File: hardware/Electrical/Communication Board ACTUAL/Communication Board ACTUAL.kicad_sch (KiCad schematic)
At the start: 14 parts, among them J1 CC1101 Radio, J2 Camera, J3 MCP9808 Temperature Sensor, Q1 2N2222, U1 STM32F411CEUx

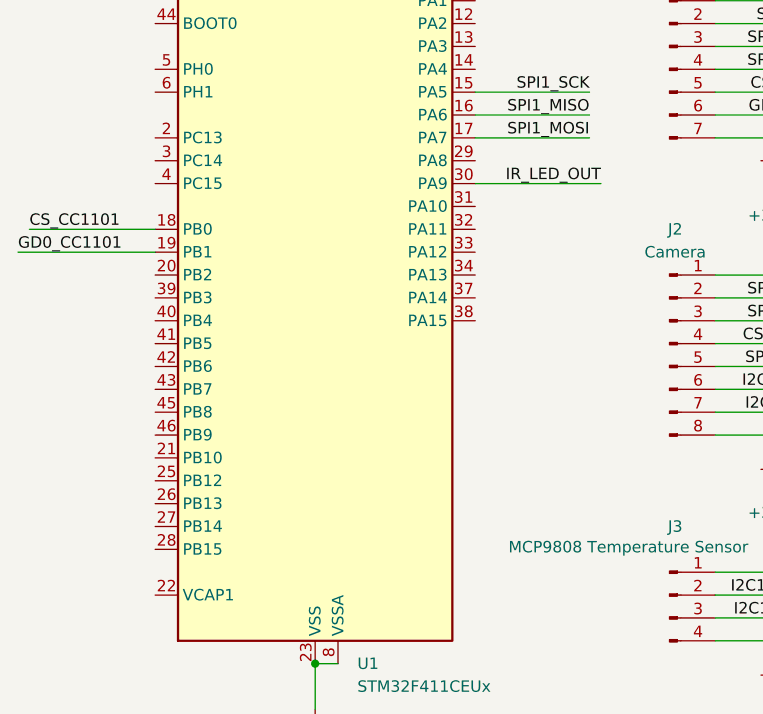
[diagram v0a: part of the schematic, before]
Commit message: changed comm board pin labels
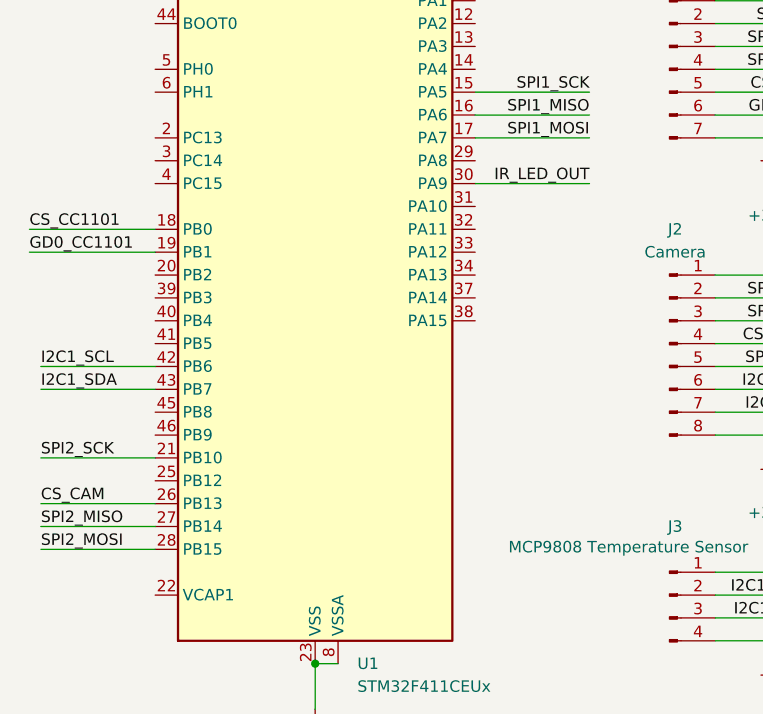
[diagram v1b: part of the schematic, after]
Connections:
- net CS_CAM: now also U1.26 (PB13)
- net I2C1_SCL: now also U1.42 (PB6)
- net I2C1_SDA: now also U1.43 (PB7)
- net SPI2_MISO: now also U1.27 (PB14)
- net SPI2_MOSI: now also U1.28 (PB15)
- net SPI2_SCK: now also U1.21 (PB10)
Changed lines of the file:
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@@
 	(wire
 		(pts
-			(xy 133.35 86.36) (xy 119.38 86.36)
+			(xy 132.08 86.36) (xy 119.38 86.36)
 		)
 		(stroke
@@
 	(wire
 		(pts
+			(xy 71.12 124.46) (xy 83.82 124.46)
+		)
+		(stroke
+			(width 0)
+			(type default)
+		)
+	)
+	(wire
+		(pts
 			(xy 152.4 114.3) (xy 152.4 116.84)
 		)
@@
 	(wire
 		(pts
+			(xy 71.12 121.92) (xy 83.82 121.92)
+		)
+		(stroke
+			(width 0)
+			(type default)
+		)
+	)
+	(wire
+		(pts
 			(xy 96.52 55.88) (xy 99.06 55.88)
 		)
@@
 	(wire
 		(pts
+			(xy 71.12 109.22) (xy 83.82 109.22)
+		)
+		(stroke
+			(width 0)
+			(type default)
+		)
+	)
+	(wire
+		(pts
 			(xy 101.6 139.7) (xy 101.6 144.78)
 		)
@@
 	(wire
 		(pts
+			(xy 71.12 116.84) (xy 83.82 116.84)
+		)
+		(stroke
+			(width 0)
+			(type default)
+		)
+	)
+	(wire
+		(pts
 			(xy 201.93 80.01) (xy 204.47 80.01)
 		)
@@
 	(wire
 		(pts
-			(xy 68.58 93.98) (xy 83.82 93.98)
+			(xy 69.85 93.98) (xy 83.82 93.98)
 		)
 		(stroke
@@
 	(wire
 		(pts
+			(xy 71.12 106.68) (xy 83.82 106.68)
+		)
+		(stroke
+			(width 0)
+			(type default)
+		)
+	)
+	(wire
+		(pts
 			(xy 99.06 55.88) (xy 101.6 55.88)
 		)
@@
 		(pts
 			(xy 195.58 121.92) (xy 195.58 124.46)
+		)
+		(stroke
+			(width 0)
+			(type default)
+		)
+	)
+	(wire
+		(pts
+			(xy 71.12 127) (xy 83.82 127)
 		)
 		(stroke
@@
 	)
 	(label "GD0_CC1101"
-		(at 68.58 93.98 0)
+		(at 69.85 93.98 0)
 		(effects
 			(font
@@
 		)
 	)
+	(label "SPI2_MOSI"
+		(at 71.12 127 0)
+		(effects
+			(font
+				(size 1.27 1.27)
+			)
+			(justify left bottom)
+		)
+	)
 	(label "SPI1_SCK"
 		(at 132.08 76.2 180)
@@
 		)
 	)
+	(label "I2C1_SDA"
+		(at 71.12 109.22 0)
+		(effects
+			(font
+				(size 1.27 1.27)
+			)
+			(justify left bottom)
+		)
+	)
 	(label "SPI1_SCK"
 		(at 158.75 68.58 180)
@@
 		)
 	)
+	(label "SPI2_MISO"
+		(at 71.12 124.46 0)
+		(effects
+			(font
+				(size 1.27 1.27)
+			)
+			(justify left bottom)
+		)
+	)
+	(label "SPI2_SCK"
+		(at 71.12 116.84 0)
+		(effects
+			(font
+				(size 1.27 1.27)
+			)
+			(justify left bottom)
+		)
+	)
+	(label "I2C1_SCL"
+		(at 71.12 106.68 0)
+		(effects
+			(font
+				(size 1.27 1.27)
+			)
+			(justify left bottom)
+		)
+	)
 	(label "GD0_CC1101"
 		(at 161.29 78.74 180)
@@
 		)
 	)
+	(label "CS_CAM"
+		(at 71.12 121.92 0)
+		(effects
+			(font
+				(size 1.27 1.27)
+			)
+			(justify left bottom)
+		)
+	)
 	(label "IR_LED_OUT"
-		(at 133.35 86.36 180)
-		(effects
-			(font
+		(at 132.08 86.36 180)
+		(effects
+			(font
